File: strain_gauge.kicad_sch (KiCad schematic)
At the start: 6 parts, among them U14 INA826

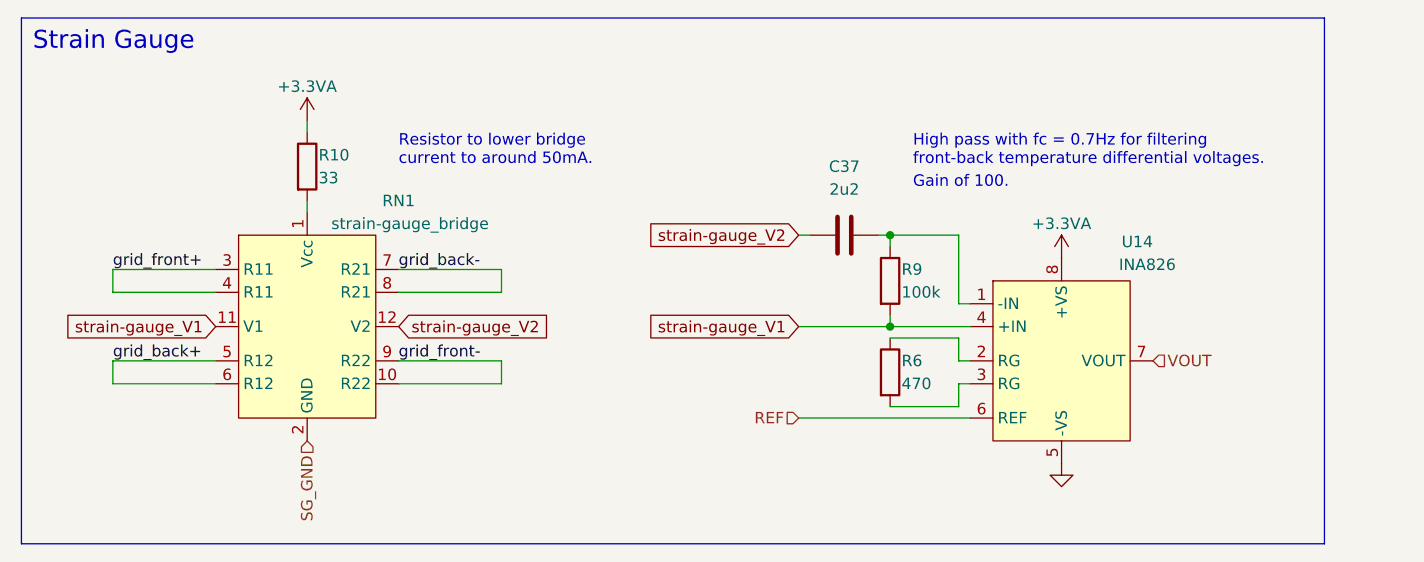
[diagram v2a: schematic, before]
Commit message: Switch from STM32F072 to STM32F103, Add fin shape draft, Place component footprints
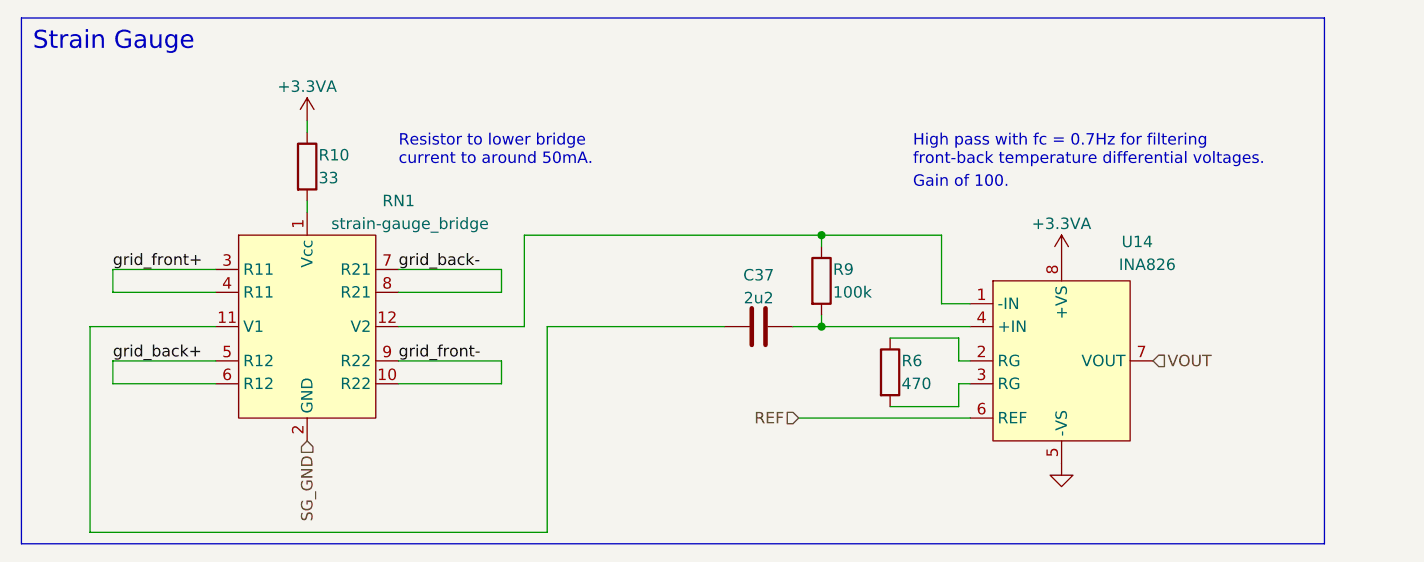
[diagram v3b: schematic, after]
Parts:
- R6: footprint Resistor_SMD:R_0402_1005Metric_Pad0.72x0.64mm_HandSolder -> Resistor_SMD:R_0603_1608Metric_Pad0.98x0.95mm_HandSolder
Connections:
- net at R9.1, U14.1 (-IN): now also RN1.12 (V2); no longer C37.2
- net strain-gauge_V1: no longer names the net of R9.2, U14.4 (+IN)
- net strain-gauge_V1: now also C37.2; no longer RN1.11 (V1)
- net strain-gauge_V2: no longer names the net of C37.1
- net strain-gauge_V2: now also RN1.11 (V1); no longer RN1.12 (V2)
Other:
- moved on the sheet: C37, R9
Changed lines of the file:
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@@
 (kicad_sch (version 20230121) (generator eeschema)
   (paper "A5")
-  (junction (at 110.49 38.1) (diameter 0) (color 0 0 0 0)
-  )
-  (junction (at 110.49 48.26) (diameter 0) (color 0 0 0 0)
-  )
-  (wire (pts (xy 110.49 48.26) (xy 110.49 46.99))
-    (stroke (width 0) (type default))
-  )
-  (wire (pts (xy 119.38 45.72) (xy 118.11 45.72))
+  (junction (at 102.87 38.1) (diameter 0) (color 0 0 0 0)
+  )
+  (junction (at 102.87 48.26) (diameter 0) (color 0 0 0 0)
+  )
+  (wire (pts (xy 102.87 46.99) (xy 102.87 48.26))
+    (stroke (width 0) (type default))
+  )
+  (wire (pts (xy 69.85 38.1) (xy 102.87 38.1))
     (stroke (width 0) (type default))
   )
@@
     (stroke (width 0) (type default))
   )
-  (wire (pts (xy 118.11 38.1) (xy 110.49 38.1))
-    (stroke (width 0) (type default))
-  )
-  (wire (pts (xy 110.49 48.26) (xy 119.38 48.26))
+  (wire (pts (xy 116.205 45.72) (xy 119.38 45.72))
+    (stroke (width 0) (type default))
+  )
+  (wire (pts (xy 69.85 48.26) (xy 69.85 38.1))
     (stroke (width 0) (type default))
   )
@@
     (stroke (width 0) (type default))
   )
-  (wire (pts (xy 100.33 38.1) (xy 101.6 38.1))
+  (wire (pts (xy 116.205 38.1) (xy 116.205 45.72))
     (stroke (width 0) (type default))
   )
@@
     (stroke (width 0) (type default))
   )
-  (wire (pts (xy 110.49 38.1) (xy 110.49 39.37))
+  (wire (pts (xy 102.87 38.1) (xy 102.87 39.37))
     (stroke (width 0) (type default))
   )
@@
     (stroke (width 0) (type default))
   )
+  (wire (pts (xy 99.695 48.26) (xy 102.87 48.26))
+    (stroke (width 0) (type default))
+  )
   (wire (pts (xy 118.11 54.61) (xy 119.38 54.61))
     (stroke (width 0) (type default))
   )
+  (wire (pts (xy 72.39 48.26) (xy 92.075 48.26))
+    (stroke (width 0) (type default))
+  )
   (wire (pts (xy 55.88 52.07) (xy 67.31 52.07))
     (stroke (width 0) (type default))
   )
+  (wire (pts (xy 102.87 48.26) (xy 119.38 48.26))
+    (stroke (width 0) (type default))
+  )
+  (wire (pts (xy 72.39 48.26) (xy 72.39 71.12))
+    (stroke (width 0) (type default))
+  )
+  (wire (pts (xy 102.87 38.1) (xy 116.205 38.1))
+    (stroke (width 0) (type default))
+  )
   (wire (pts (xy 67.31 54.61) (xy 55.88 54.61))
     (stroke (width 0) (type default))
@@
     (stroke (width 0) (type default))
   )
+  (wire (pts (xy 35.56 48.26) (xy 21.59 48.26))
+    (stroke (width 0) (type default))
+  )
   (wire (pts (xy 24.13 41.91) (xy 35.56 41.91))
     (stroke (width 0) (type default))
@@
     (stroke (width 0) (type default))
   )
-  (wire (pts (xy 100.33 48.26) (xy 110.49 48.26))
-    (stroke (width 0) (type default))
-  )
   (wire (pts (xy 118.11 57.15) (xy 118.11 54.61))
     (stroke (width 0) (type default))
   )
+  (wire (pts (xy 21.59 48.26) (xy 21.59 71.12))
+    (stroke (width 0) (type default))
+  )
   (wire (pts (xy 24.13 54.61) (xy 35.56 54.61))
     (stroke (width 0) (type default))
   )
-  (wire (pts (xy 109.22 38.1) (xy 110.49 38.1))
-    (stroke (width 0) (type default))
-  )
   (wire (pts (xy 55.88 41.91) (xy 67.31 41.91))
     (stroke (width 0) (type default))
   )
+  (wire (pts (xy 21.59 71.12) (xy 72.39 71.12))
+    (stroke (width 0) (type default))
+  )
   (wire (pts (xy 67.31 41.91) (xy 67.31 44.45))
     (stroke (width 0) (type default))
   )
-  (wire (pts (xy 118.11 45.72) (xy 118.11 38.1))
+  (wire (pts (xy 55.88 48.26) (xy 69.85 48.26))
     (stroke (width 0) (type default))
   )
@@
   (label "grid_back-" (at 55.88 41.91 0) (fields_autoplaced)
     (effects (font (size 1.27 1.27)) (justify left bottom))
-  )
-  (global_label "strain-gauge_V2" (shape input) (at 55.88 48.26 0) (fields_autoplaced)
-    (effects (font (size 1.27 1.27)) (justify left))
-    (property "Intersheetrefs" "${INTERSHEET_REFS}" (at 74.8307 48.26 0)
-      (effects (font (size 1.27 1.27)) (justify left) hide)
-    )
-  )
-  (global_label "strain-gauge_V1" (shape input) (at 100.33 48.26 180) (fields_autoplaced)
-    (effects (font (size 1.27 1.27)) (justify right))
-    (property "Intersheetrefs" "${INTERSHEET_REFS}" (at 81.3793 48.26 0)
-      (effects (font (size 1.27 1.27)) (justify right) hide)
-    )
-  )
-  (global_label "strain-gauge_V1" (shape input) (at 35.56 48.26 180) (fields_autoplaced)
-    (effects (font (size 1.27 1.27)) (justify right))
-    (property "Intersheetrefs" "${INTERSHEET_REFS}" (at 16.6093 48.26 0)
-      (effects (font (size 1.27 1.27)) (justify right) hide)
-    )
-  )
-  (global_label "strain-gauge_V2" (shape input) (at 100.33 38.1 180) (fields_autoplaced)
-    (effects (font (size 1.27 1.27)) (justify right))
-    (property "Intersheetrefs" "${INTERSHEET_REFS}" (at 81.3793 38.1 0)
-      (effects (font (size 1.27 1.27)) (justify right) hide)
-    )
   )
   (hierarchical_label "REF" (shape input) (at 100.33 58.42 180) (fields_autoplaced)
@@
     )
   )
-  (symbol (lib_id "Device:R") (at 110.49 43.18 0) (unit 1)
-    (in_bom yes) (on_board yes) (dnp no)
-    (property "Reference" "R9" (at 111.76 41.91 0)
-      (effects (font (size 1.27 1.27)) (justify left))
-    )
-    (property "Value" "100k" (at 111.76 44.45 0)
-      (effects (font (size 1.27 1.27)) (justify left))
-    )
-    (property "Footprint" "Resistor_SMD:R_0402_1005Metric_Pad0.72x0.64mm_HandSolder" (at 108.712 43.18 90)
-      (effects (font (size 1.27 1.27)) hide)
-    )
-    (property "Datasheet" "~" (at 110.49 43.18 0)
+  (symbol (lib_id "Device:R") (at 102.87 43.18 0) (unit 1)
+    (in_bom yes) (on_board yes) (dnp no)
+    (property "Reference" "R9" (at 104.14 41.91 0)
+      (effects (font (size 1.27 1.27)) (justify left))
+    )
+    (property "Value" "100k" (at 104.14 44.45 0)
+      (effects (font (size 1.27 1.27)) (justify left))
+    )
+    (property "Footprint" "Resistor_SMD:R_0402_1005Metric_Pad0.72x0.64mm_HandSolder" (at 101.092 43.18 90)
+      (effects (font (size 1.27 1.27)) hide)
+    )
+    (property "Datasheet" "~" (at 102.87 43.18 0)
       (effects (font (size 1.27 1.27)) hide)
     )
@@
       (effects (font (size 1.27 1.27)) (justify left))
     )
-    (property "Footprint" "Resistor_SMD:R_0402_1005Metric_Pad0.72x0.64mm_HandSolder" (at 108.712 53.34 90)
+    (property "Footprint" "Resistor_SMD:R_0603_1608Metric_Pad0.98x0.95mm_HandSolder" (at 108.712 53.34 90)
       (effects (font (size 1.27 1.27)) hide)
     )
@@
     )
   )
-  (symbol (lib_id "Device:C") (at 105.41 38.1 90) (unit 1)
-    (in_bom yes) (on_board yes) (dnp no) (fields_autoplaced)
-    (property "Reference" "C37" (at 105.41 30.48 90)
+  (symbol (lib_id "Device:C") (at 95.885 48.26 90) (unit 1)
+    (in_bom yes) (on_board yes) (dnp no)
+    (property "Reference" "C37" (at 95.885 42.545 90)
       (effects (font (size 1.27 1.27)))
     )
-    (property "Value" "2u2" (at 105.41 33.02 90)
+    (property "Value" "2u2" (at 95.885 45.085 90)
       (effects (font (size 1.27 1.27)))
     )
-    (property "Footprint" "Capacitor_SMD:C_0603_1608Metric_Pad1.08x0.95mm_HandSolder" (at 109.22 37.1348 0)
-      (effects (font (size 1.27 1.27)) hide)
-    )
-    (property "Datasheet" "~" (at 105.41 38.1 0)
-      (effects (font (size 1.27 1.27)) hide)
-    )
+    (property "Footprint" "Capacitor_SMD:C_0603_1608Metric_Pad1.08x0.95mm_HandSolder" (at 99.695 47.2948 0)
+      (effects (font (size 1.27 1.27)) hide)
+    )
+    (property "Datasheet" "~" (at 95.885 48.26 0)
+      (effects (font (size 1.27 1.27)) hide)
+    )

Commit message: PCB Layout (traces, edge cuts, silk screen, 3d models)
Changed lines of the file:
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@@
-    (stroke (width 0) (type default))
-  )
-  (wire (pts (xy 67.31 44.45) (xy 55.88 44.45))
     (stroke (width 0) (type default))
   )
@@
     (stroke (width 0) (type default))
   )
-  (wire (pts (xy 67.31 54.61) (xy 55.88 54.61))
+  (wire (pts (xy 55.88 44.45) (xy 67.31 44.45))
+    (stroke (width 0) (type default))
+  )
+  (wire (pts (xy 55.88 54.61) (xy 67.31 54.61))
     (stroke (width 0) (type default))
   )
@@
     (effects (font (size 1.27 1.27)) (justify left))
   )
+  (netclass_flag "" (length 2.54) (shape round) (at 67.31 44.45 180)
+    (effects (font (size 1.27 1.27)) (justify right bottom))
+    (property "Netclass" "grid" (at 62.23 46.355 0)
+      (effects (font (size 1.27 1.27) italic) (justify left))
+    )
+  )
+  (netclass_flag "" (length 2.54) (shape round) (at 67.31 54.61 180)
+    (effects (font (size 1.27 1.27)) (justify right bottom))
+    (property "Netclass" "grid" (at 62.23 56.515 0)
+      (effects (font (size 1.27 1.27) italic) (justify left))
+    )
+  )
+  (netclass_flag "" (length 2.54) (shape round) (at 24.13 54.61 180)
+    (effects (font (size 1.27 1.27)) (justify right bottom))
+    (property "Netclass" "grid" (at 25.4 56.515 0)
+      (effects (font (size 1.27 1.27) italic) (justify left))
+    )
+  )
+  (netclass_flag "" (length 2.54) (shape round) (at 24.13 44.45 180)
+    (effects (font (size 1.27 1.27)) (justify right bottom))
+    (property "Netclass" "grid" (at 25.4 46.355 0)
+      (effects (font (size 1.27 1.27) italic) (justify left))
+    )
+  )
   (symbol (lib_id "power:+3.3VA") (at 45.72 25.4 0) (unit 1)

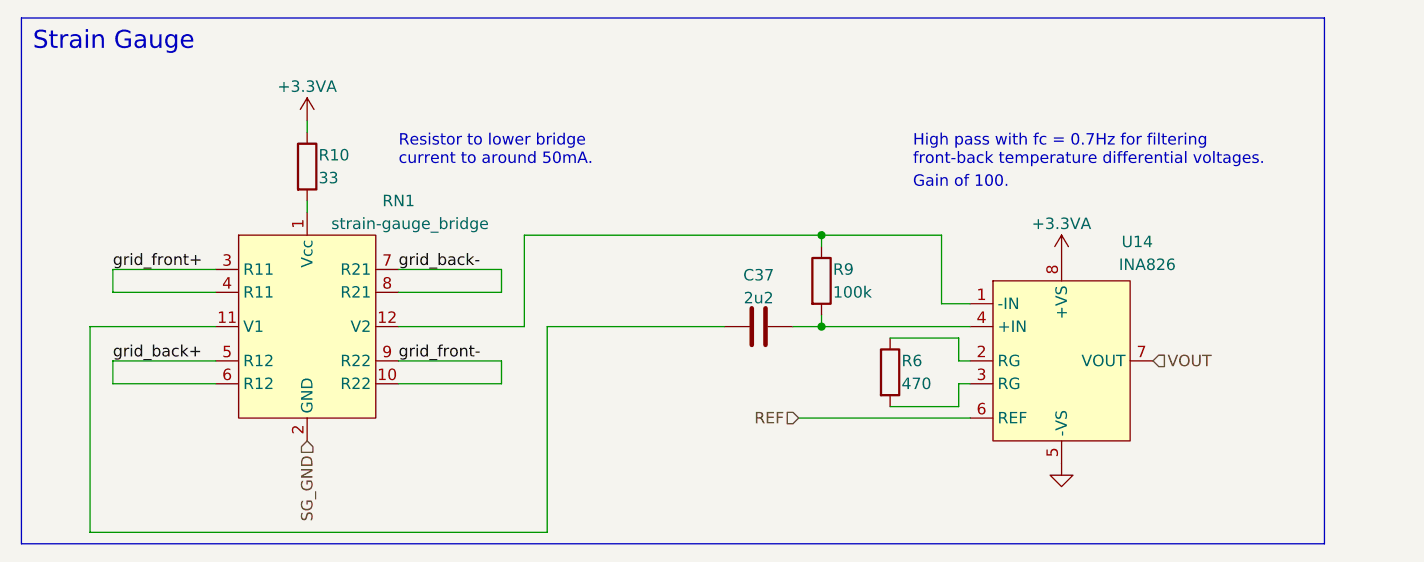
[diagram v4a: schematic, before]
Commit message: implement changes from rev 0 to rev 1
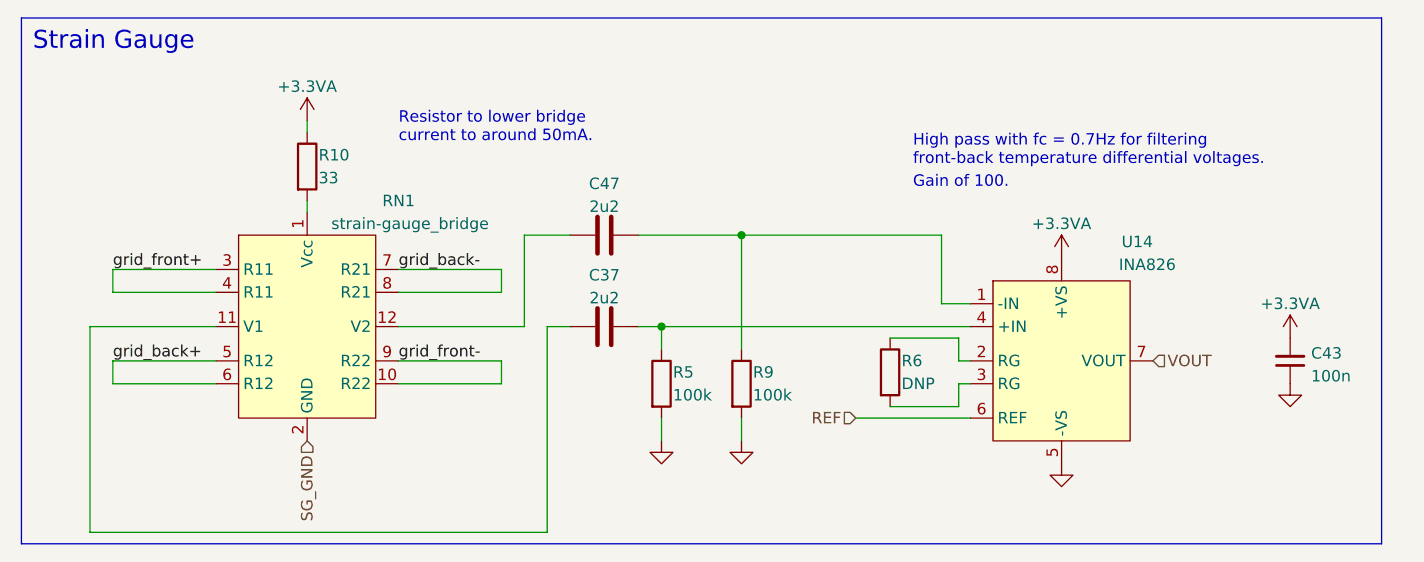
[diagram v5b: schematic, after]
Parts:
- added C43: 100n, Capacitor_SMD:C_0402_1005Metric_Pad0.74x0.62mm_HandSolder, symbol Device:C_Small
- added C47: 2u2, Capacitor_SMD:C_0603_1608Metric_Pad1.08x0.95mm_HandSolder, symbol Device:C
- added R5: 100k, Resistor_SMD:R_0402_1005Metric_Pad0.72x0.64mm_HandSolder, symbol Device:R
- R6: value 470 -> DNP
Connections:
- net +3.3VA: now also C43.2
- net GND: now also R9.2, C43.1, R5.2
- net at R9.1, U14.1 (-IN): now also C47.2; no longer RN1.12 (V2)
- net at C37.2, U14.4 (+IN): now also R5.1; no longer R9.2
- new net: C47.1, RN1.12 (V2)
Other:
- moved on the sheet: C37, R9

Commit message: add LCSC part numbers, tweak some footprints
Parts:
- C37, C47: LCSC# (none) -> C23630
- C43: LCSC# (none) -> C307331
- R10: footprint Resistor_SMD:R_0402_1005Metric_Pad0.72x0.64mm_HandSolder -> Resistor_SMD:R_0603_1608Metric_Pad0.98x0.95mm_HandSolder; LCSC# (none) -> C23140; Manufacturer (none) -> UNI-ROYAL(Uniroyal Elec); Notes (none) -> TOO HIGH CURRENT!
- R5, R9: LCSC# (none) -> C25741; Manufacturer (none) -> UNI-ROYAL(Uniroyal Elec)
- U14: LCSC# (none) -> C38433; Manufacturer (none) -> Texas Instruments
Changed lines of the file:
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@@
+      (effects (font (size 1.27 1.27)) hide)
+    )
+    (property "LCSC#" "C25741" (at 93.98 54.61 0)
+      (effects (font (size 1.27 1.27)) hide)
+    )
+    (property "Manufacturer" "UNI-ROYAL(Uniroyal Elec)" (at 93.98 54.61 0)
       (effects (font (size 1.27 1.27)) hide)
     )
@@
     )
     (property "Datasheet" "~" (at 85.09 54.61 0)
+      (effects (font (size 1.27 1.27)) hide)
+    )
+    (property "LCSC#" "C25741" (at 85.09 54.61 0)
+      (effects (font (size 1.27 1.27)) hide)
+    )
+    (property "Manufacturer" "UNI-ROYAL(Uniroyal Elec)" (at 85.09 54.61 0)
       (effects (font (size 1.27 1.27)) hide)
     )
@@
       (effects (font (size 1.27 1.27)) hide)
     )
-    (property "LCSC#" "" (at 154.94 52.07 0)
+    (property "LCSC#" "C307331" (at 154.94 52.07 0)
       (effects (font (size 1.27 1.27)) hide)
     )
@@
     )
     (property "Datasheet" "" (at 148.59 29.21 0)
+      (effects (font (size 1.27 1.27)) hide)
+    )
+    (property "LCSC#" "C38433" (at 129.54 52.07 0)
+      (effects (font (size 1.27 1.27)) hide)
+    )
+    (property "Manufacturer" "Texas Instruments" (at 129.54 52.07 0)
       (effects (font (size 1.27 1.27)) hide)
     )
@@
       (effects (font (size 1.27 1.27)) hide)
     )
+    (property "LCSC#" "C23630" (at 78.74 38.1 0)
+      (effects (font (size 1.27 1.27)) hide)
+    )
     (pin "1")
     (pin "2")
@@
       (effects (font (size 1.27 1.27)) (justify left))
     )
-    (property "Footprint" "Resistor_SMD:R_0402_1005Metric_Pad0.72x0.64mm_HandSolder" (at 43.942 30.48 90)
+    (property "Footprint" "Resistor_SMD:R_0603_1608Metric_Pad0.98x0.95mm_HandSolder" (at 43.942 30.48 90)
       (effects (font (size 1.27 1.27)) hide)
     )
@@
       (effects (font (size 1.27 1.27)) hide)
     )
+    (property "Notes" "TOO HIGH CURRENT!" (at 45.72 30.48 0)
+      (effects (font (size 1.27 1.27)) hide)
+    )
+    (property "Manufacturer" "UNI-ROYAL(Uniroyal Elec)" (at 45.72 30.48 0)
+      (effects (font (size 1.27 1.27)) hide)
+    )
+    (property "LCSC#" "C23140" (at 45.72 30.48 0)
+      (effects (font (size 1.27 1.27)) hide)
+    )
     (pin "1")
     (pin "2")
@@
       (effects (font (size 1.27 1.27)) hide)
     )
+    (property "LCSC#" "C23630" (at 78.74 48.26 0)
+      (effects (font (size 1.27 1.27)) hide)
+    )
